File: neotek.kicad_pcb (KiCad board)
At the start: 2 copper layers, 18 parts, among them P1 USB_OTG, U1 STM32F103C4, U2 MIC5219-3.3, Y1 Crystal

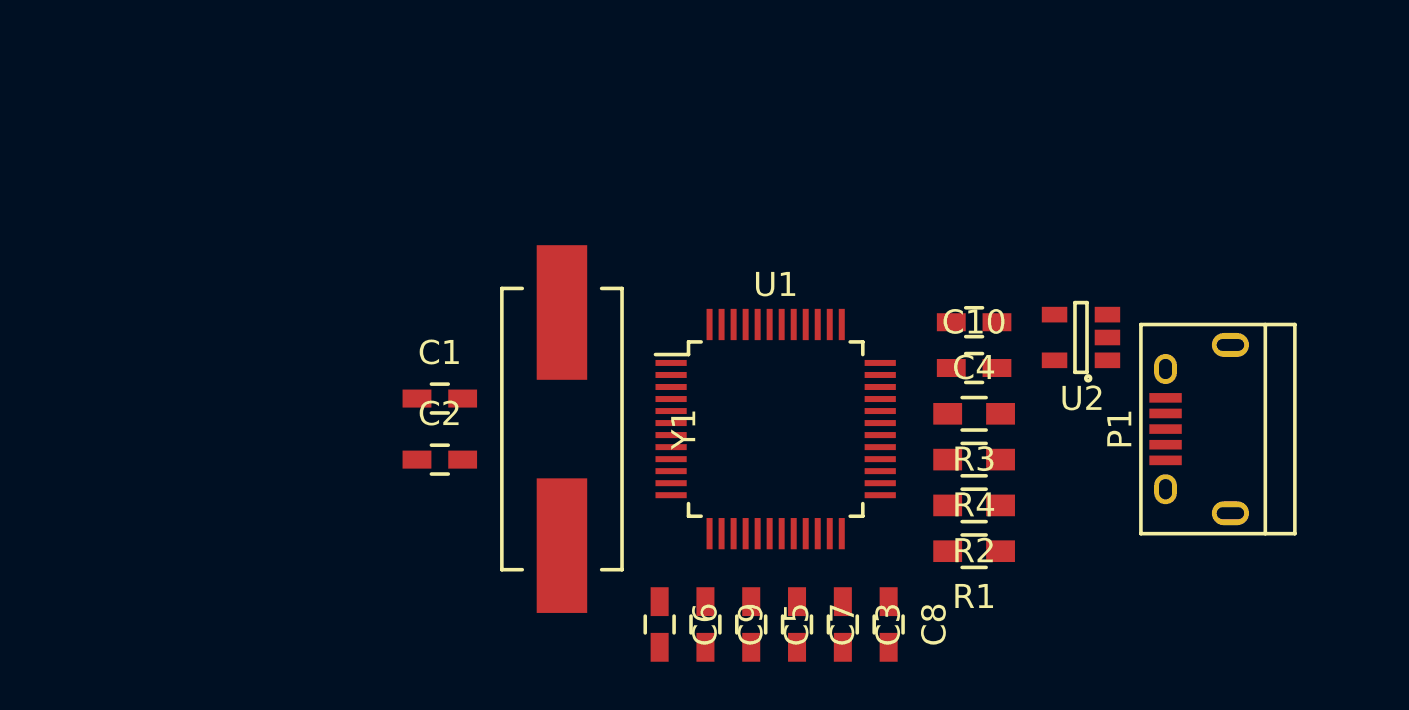
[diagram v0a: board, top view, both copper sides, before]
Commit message: Added headers; made footprint & layout stub
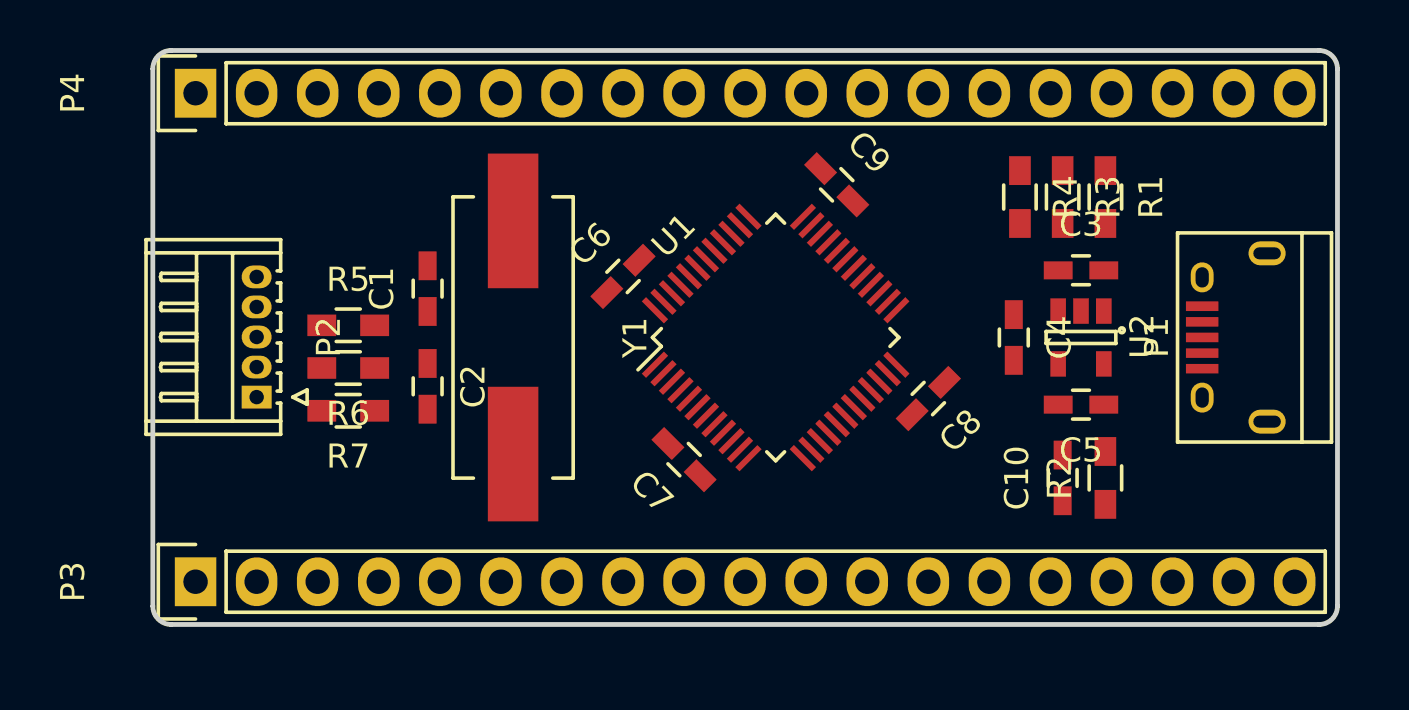
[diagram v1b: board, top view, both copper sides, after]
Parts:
- added P2: CONN_01X05, Connectors_Hirose:Hirose_DF13-05P-1.25DS_05x1.25mm_Angled, F.Cu at (111.8, 91.4)
- added P3: CONN_01X19, Pin_Headers:Pin_Header_Straight_1x19, F.Cu at (109.2, 99.1)
- added P4: CONN_01X19, Pin_Headers:Pin_Header_Straight_1x19, F.Cu at (109.2, 78.7)
- added R5: 10k, Resistors_SMD:R_0603_HandSoldering, F.Cu at (115.6, 88.4)
- added R6: 10k, Resistors_SMD:R_0603_HandSoldering, F.Cu at (115.6, 90.2)
- added R7: 10k, Resistors_SMD:R_0603_HandSoldering, F.Cu at (115.6, 91.9)
- moved C9 19.1 mm to (135.9, 82.5), turned to 315 degrees
- moved C3 17.8 mm to (146.1, 86.1), turned to 0 degrees
- moved C5 16.5 mm to (146.1, 91.7), turned to 180 degrees
- moved R1 15.7 mm to (147.1, 83.1), turned to 270 degrees
- moved C6 14.6 mm to (127.0, 86.4), turned to 45 degrees
- moved R4 11.1 mm to (143.5, 83.1), turned to 270 degrees
- moved R3 9.74 mm to (145.3, 83.1), turned to 270 degrees
- moved C8 9.54 mm to (139.7, 91.4), turned to 225 degrees
- moved C7 8.31 mm to (129.5, 94.0), turned to 135 degrees
- moved C10 5.87 mm to (145.3, 94.7), turned to 90 degrees
- moved R2 5.58 mm to (147.1, 94.7), turned to 90 degrees
- moved C1 4.60 mm to (118.9, 86.9), turned to 90 degrees
- moved Y1 4.32 mm to (122.4, 88.9)
- moved P1 4.10 mm to (152.7, 88.9)
- moved U1 3.81 mm to (133.3, 88.9), turned to 45 degrees
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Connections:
- net Net-(U1-Pad44) renamed /BOOT0
- U1 pad 10: Net-(U1-Pad10) -> /PA0
- U1 pad 11: Net-(U1-Pad11) -> /PA1
- U1 pad 12: Net-(U1-Pad12) -> /PA2
- U1 pad 13: Net-(U1-Pad13) -> /PA3
- U1 pad 14: Net-(U1-Pad14) -> /PA4
- U1 pad 15: Net-(U1-Pad15) -> /PA5
- U1 pad 16: Net-(U1-Pad16) -> /PA6
- U1 pad 17: Net-(U1-Pad17) -> /PA7
- U1 pad 18: Net-(U1-Pad18) -> /PB0
- U1 pad 19: Net-(U1-Pad19) -> /PB1
- U1 pad 2: Net-(U1-Pad2) -> /PC13
- U1 pad 20: Net-(U1-Pad20) -> /PB2
- U1 pad 21: Net-(U1-Pad21) -> /PB10
- U1 pad 22: Net-(U1-Pad22) -> /PB11
- U1 pad 23: +3V3 -> GND
- U1 pad 25: Net-(U1-Pad25) -> /PB12
- U1 pad 26: Net-(U1-Pad26) -> /PB13
- U1 pad 27: Net-(U1-Pad27) -> /PB14
- U1 pad 28: Net-(U1-Pad28) -> /PB15
- U1 pad 29: Net-(U1-Pad29) -> /PA8
- U1 pad 3: Net-(U1-Pad3) -> /PC14
- U1 pad 30: Net-(U1-Pad30) -> /PA9
- U1 pad 31: Net-(U1-Pad31) -> /PA10
- U1 pad 34: Net-(U1-Pad34) -> SWDIO
- U1 pad 35: +3V3 -> GND
- U1 pad 37: Net-(U1-Pad37) -> SWDCLK
- U1 pad 38: Net-(U1-Pad38) -> /PA15
- U1 pad 39: Net-(U1-Pad39) -> /PB3
- U1 pad 4: Net-(U1-Pad4) -> /PC15
- U1 pad 40: Net-(U1-Pad40) -> /PB4
- U1 pad 41: Net-(U1-Pad41) -> /PB5
- U1 pad 42: Net-(U1-Pad42) -> /PB6
- U1 pad 43: Net-(U1-Pad43) -> /PB7
- U1 pad 45: Net-(U1-Pad45) -> /PB8
- U1 pad 46: Net-(U1-Pad46) -> /PB9
- U1 pad 47: +3V3 -> GND
- U1 pad 7: Net-(U1-Pad7) -> NRST
- U1 pad 8: +3V3 -> GND
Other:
- board outline added: 49.3 x 23.9 mm

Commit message: wip
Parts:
- P1: footprint Connect:USB_Micro-B -> Connect:USB_Micro-B_10103594-0001LF
- moved P1 0.76 mm to (153.4, 88.9)
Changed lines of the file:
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@@
-(kicad_pcb (version 4) (host pcbnew 4.0.4+dfsg1-stable)
+(kicad_pcb (version 4) (host pcbnew 4.0.2+dfsg1-stable)
   (general
-    (links 94)
-    (no_connects 94)
-    (area 103.145 73.706666 158.529 104.093333)
+    (links 96)
+    (no_connects 96)
+    (area 107.341999 76.861999 156.818001 100.938001)
     (thickness 1.6)
     (drawings 8)
@@
     )
   )
-  (module Connect:USB_Micro-B (layer F.Cu)
-    (at 152.654 88.8991 90)
-    (descr "Micro USB Type B Receptacle")
-    (tags "USB USB_B USB_micro USB_OTG")
-    (attr smd)
-    (fp_text reference P1 (at 0 -3.45 90) (layer F.SilkS)
-      (effects (font (size 1 1) (thickness 0.15)))
-    )
-    (fp_text value USB_OTG (at 0 4.8 90) (layer F.Fab)
-      (effects (font (size 1 1) (thickness 0.15)))
-    )
-    (fp_line (start -4.6 -2.8) (end 4.6 -2.8) (layer F.CrtYd) (width 0.05))
-    (fp_line (start 4.6 -2.8) (end 4.6 4.05) (layer F.CrtYd) (width 0.05))
-    (fp_line (start 4.6 4.05) (end -4.6 4.05) (layer F.CrtYd) (width 0.05))
-    (fp_line (start -4.6 4.05) (end -4.6 -2.8) (layer F.CrtYd) (width 0.05))
-    (fp_line (start -4.3509 3.81746) (end 4.3491 3.81746) (layer F.SilkS) (width 0.15))
-    (fp_line (start -4.3509 -2.58754) (end 4.3491 -2.58754) (layer F.SilkS) (width 0.15))
-    (fp_line (start 4.3491 -2.58754) (end 4.3491 3.81746) (layer F.SilkS) (width 0.15))
-    (fp_line (start 4.3491 2.58746) (end -4.3509 2.58746) (layer F.SilkS) (width 0.15))
-    (fp_line (start -4.3509 3.81746) (end -4.3509 -2.58754) (layer F.SilkS) (width 0.15))
-    (pad 1 smd rect (at -1.3009 -1.56254 180) (size 1.35 0.4) (layers F.Cu F.Paste F.Mask)
-      (net 4 +5V))
-    (pad 2 smd rect (at -0.6509 -1.56254 180) (size 1.35 0.4) (layers F.Cu F.Paste F.Mask)
-      (net 7 "Net-(P1-Pad2)"))
-    (pad 3 smd rect (at -0.0009 -1.56254 180) (size 1.35 0.4) (layers F.Cu F.Paste F.Mask)
-      (net 8 "Net-(P1-Pad3)"))
-    (pad 4 smd rect (at 0.6491 -1.56254 180) (size 1.35 0.4) (layers F.Cu F.Paste F.Mask)
-      (net 9 "Net-(P1-Pad4)"))
-    (pad 5 smd rect (at 1.2991 -1.56254 180) (size 1.35 0.4) (layers F.Cu F.Paste F.Mask)
-      (net 1 GND))
-    (pad 6 thru_hole oval (at -2.5009 -1.56254 180) (size 0.95 1.25) (drill oval 0.55 0.85) (layers *.Cu *.Mask F.SilkS)
-      (net 10 "Net-(P1-Pad6)"))
-    (pad 6 thru_hole oval (at 2.4991 -1.56254 180) (size 0.95 1.25) (drill oval 0.55 0.85) (layers *.Cu *.Mask F.SilkS)
-      (net 10 "Net-(P1-Pad6)"))
-    (pad 6 thru_hole oval (at -3.5009 1.13746 180) (size 1.55 1) (drill oval 1.15 0.5) (layers *.Cu *.Mask F.SilkS)
-      (net 10 "Net-(P1-Pad6)"))
-    (pad 6 thru_hole oval (at 3.4991 1.13746 180) (size 1.55 1) (drill oval 1.15 0.5) (layers *.Cu *.Mask F.SilkS)
-      (net 10 "Net-(P1-Pad6)"))
-  )
   (module Resistors_SMD:R_0603_HandSoldering (layer F.Cu)
     (at 147.066 83.058 270)
@@
     )
   )
+  (module Connect:USB_Micro-B_10103594-0001LF (layer F.Cu)
+    (at 153.416 88.9 90)
+    (descr "Micro USB Type B 10103594-0001LF")
+    (tags "USB USB_B USB_micro USB_OTG")
+    (attr smd)
+    (fp_text reference P1 (at -1.5 -4.625 90) (layer F.SilkS)
+      (effects (font (size 1 1) (thickness 0.15)))
+    )
+    (fp_text value USB_OTG (at 0 6.175 90) (layer F.Fab)
+      (effects (font (size 1 1) (thickness 0.15)))
+    )
+    (fp_line (start -4.25 -3.4) (end 4.25 -3.4) (layer F.CrtYd) (width 0.05))
+    (fp_line (start 4.25 -3.4) (end 4.25 4.45) (layer F.CrtYd) (width 0.05))
+    (fp_line (start 4.25 4.45) (end -4.25 4.45) (layer F.CrtYd) (width 0.05))
+    (fp_line (start -4.25 4.45) (end -4.25 -3.4) (layer F.CrtYd) (width 0.05))
+    (fp_line (start -4 4.195) (end 4 4.195) (layer F.SilkS) (width 0.15))
+    (fp_line (start -4 -3.125) (end 4 -3.125) (layer F.SilkS) (width 0.15))
+    (fp_line (start 4 -3.125) (end 4 4.195) (layer F.SilkS) (width 0.15))
+    (fp_line (start 4 3.575) (end -4 3.575) (layer F.SilkS) (width 0.15))
+    (fp_line (start -4 4.195) (end -4 -3.125) (layer F.SilkS) (width 0.15))
+    (pad 1 smd rect (at -1.3 -1.5 180) (size 1.65 0.4) (layers F.Cu F.Paste F.Mask)
+      (net 4 +5V))
+    (pad 2 smd rect (at -0.65 -1.5 180) (size 1.65 0.4) (layers F.Cu F.Paste F.Mask)
+      (net 7 "Net-(P1-Pad2)"))
+    (pad 3 smd rect (at -0.0009 -1.5 180) (size 1.65 0.4) (layers F.Cu F.Paste F.Mask)
+      (net 8 "Net-(P1-Pad3)"))
+    (pad 4 smd rect (at 0.65 -1.5 180) (size 1.65 0.4) (layers F.Cu F.Paste F.Mask)
+      (net 9 "Net-(P1-Pad4)"))
+    (pad 5 smd rect (at 1.3 -1.5 180) (size 1.65 0.4) (layers F.Cu F.Paste F.Mask)
+      (net 1 GND))
+    (pad 6 thru_hole oval (at -2.425 -1.625 180) (size 1.5 1.1) (drill oval 1.05 0.65) (layers *.Cu *.Mask F.SilkS)
+      (net 10 "Net-(P1-Pad6)"))
+    (pad 6 thru_hole oval (at 2.425 -1.625 180) (size 1.5 1.1) (drill oval 1.05 0.65) (layers *.Cu *.Mask F.SilkS)
+      (net 10 "Net-(P1-Pad6)"))
+    (pad 6 thru_hole oval (at -2.725 1.375 180) (size 1.7 1.2) (drill oval 1.2 0.7) (layers *.Cu *.Mask F.SilkS)
+      (net 10 "Net-(P1-Pad6)"))
+    (pad 6 thru_hole oval (at 2.725 1.375 180) (size 1.7 1.2) (drill oval 1.2 0.7) (layers *.Cu *.Mask F.SilkS)
+      (net 10 "Net-(P1-Pad6)"))
+    (pad 6 smd rect (at -0.9625 1.625 180) (size 2.5 1.425) (layers F.Cu F.Paste F.Mask)
+      (net 10 "Net-(P1-Pad6)"))
+    (pad 6 smd rect (at 0.9625 1.625 180) (size 2.5 1.425) (layers F.Cu F.Paste F.Mask)
+      (net 10 "Net-(P1-Pad6)"))
+  )
   (gr_line (start 107.442 100.076) (end 107.442 77.724) (layer Edge.Cuts) (width 0.2))
